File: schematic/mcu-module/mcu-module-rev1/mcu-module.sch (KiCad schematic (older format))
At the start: 22 parts, among them P1 MCU1, P2 MICROSD-SDIO-CD, P3 SWD, P4 MCU2, U1 STM32F103RE, X1 32768Hz, X2 8MHz

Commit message: MCU connectors created
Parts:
- removed P1: MCU1, ~, symbol CONN_20
- removed P4: MCU2, ~, symbol CONN_20
- added P1: MCU1, ~, symbol MCU1
- added P4: MCU2, ~, symbol MCU2
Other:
- moved on the sheet: C1, C10, C2, C3, C4, C5, C6, C7, C8, C9, P2, P3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

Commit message: MCU module rev2 done
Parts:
- added FB1: FILTER, ~, symbol FILTER
- C2, C3: value 100pF -> 20pF
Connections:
- net +3.3V: now also FB1.2; no longer P1.2 (P2)
- new net: FB1.1, P1.2 (P2)
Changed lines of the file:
@@
 Sheet 1 1
 Title "Caustic LT MCU boart"
-Date "27 may 2015"
+Date "14 nov 2015"
 Rev "1.0"
 Comp ""
@@
 P 5950 3400
 F 0 "C2" H 5950 3500 40  0000 L CNN
-F 1 "100pF" H 5956 3315 40  0000 L CNN
+F 1 "20pF" H 5956 3315 40  0000 L CNN
 F 2 "~" H 5988 3250 30  0000 C CNN
 F 3 "~" H 5950 3400 60  0000 C CNN
@@
 P 5950 3650
 F 0 "C3" H 5950 3750 40  0000 L CNN
-F 1 "100pF" H 5956 3565 40  0000 L CNN
+F 1 "20pF" H 5956 3565 40  0000 L CNN
 F 2 "~" H 5988 3500 30  0000 C CNN
 F 3 "~" H 5950 3650 60  0000 C CNN
@@
 L +3.3V #PWR014
 U 1 1 55643F60
-P 4650 1700
-F 0 "#PWR014" H 4650 1660 30  0001 C CNN
-F 1 "+3.3V" H 4650 1810 30  0000 C CNN
-F 2 "" H 4650 1700 60  0000 C CNN
-F 3 "" H 4650 1700 60  0000 C CNN
-	1    4650 1700
+P 5050 800
+F 0 "#PWR014" H 5050 760 30  0001 C CNN
+F 1 "+3.3V" H 5050 910 30  0000 C CNN
+F 2 "" H 5050 800 60  0000 C CNN
+F 3 "" H 5050 800 60  0000 C CNN
+	1    5050 800
 	0    1    1    0
 $EndComp
@@
 	5950 5450 6100 5450
 Connection ~ 6000 5450
-Wire Wire Line
-	5550 5450 5450 5450
 Connection ~ 5450 5450
 Wire Wire Line
@@
 	5850 2100 4350 2100
 Wire Wire Line
-	4350 1700 4650 1700
+	4350 1700 4900 1700
 Wire Wire Line
 	4350 1600 4450 1600
@@
 	1    0    0    -1
 $EndComp
+Wire Wire Line
+	5550 5450 5450 5450
+$Comp
+L FILTER FB1
+U 1 1 564783BA
+P 4900 1250
+F 0 "FB1" H 4900 1400 60  0000 C CNN
+F 1 "FILTER" H 4900 1150 60  0000 C CNN
+F 2 "~" H 4900 1250 60  0000 C CNN
+F 3 "~" H 4900 1250 60  0000 C CNN
+	1    4900 1250
+	0    -1   -1   0
+$EndComp
+Wire Wire Line
+	4900 1700 4900 1600
+Wire Wire Line
+	4900 900  4900 800
+Wire Wire Line
+	4900 800  5050 800
 $EndSCHEMATC

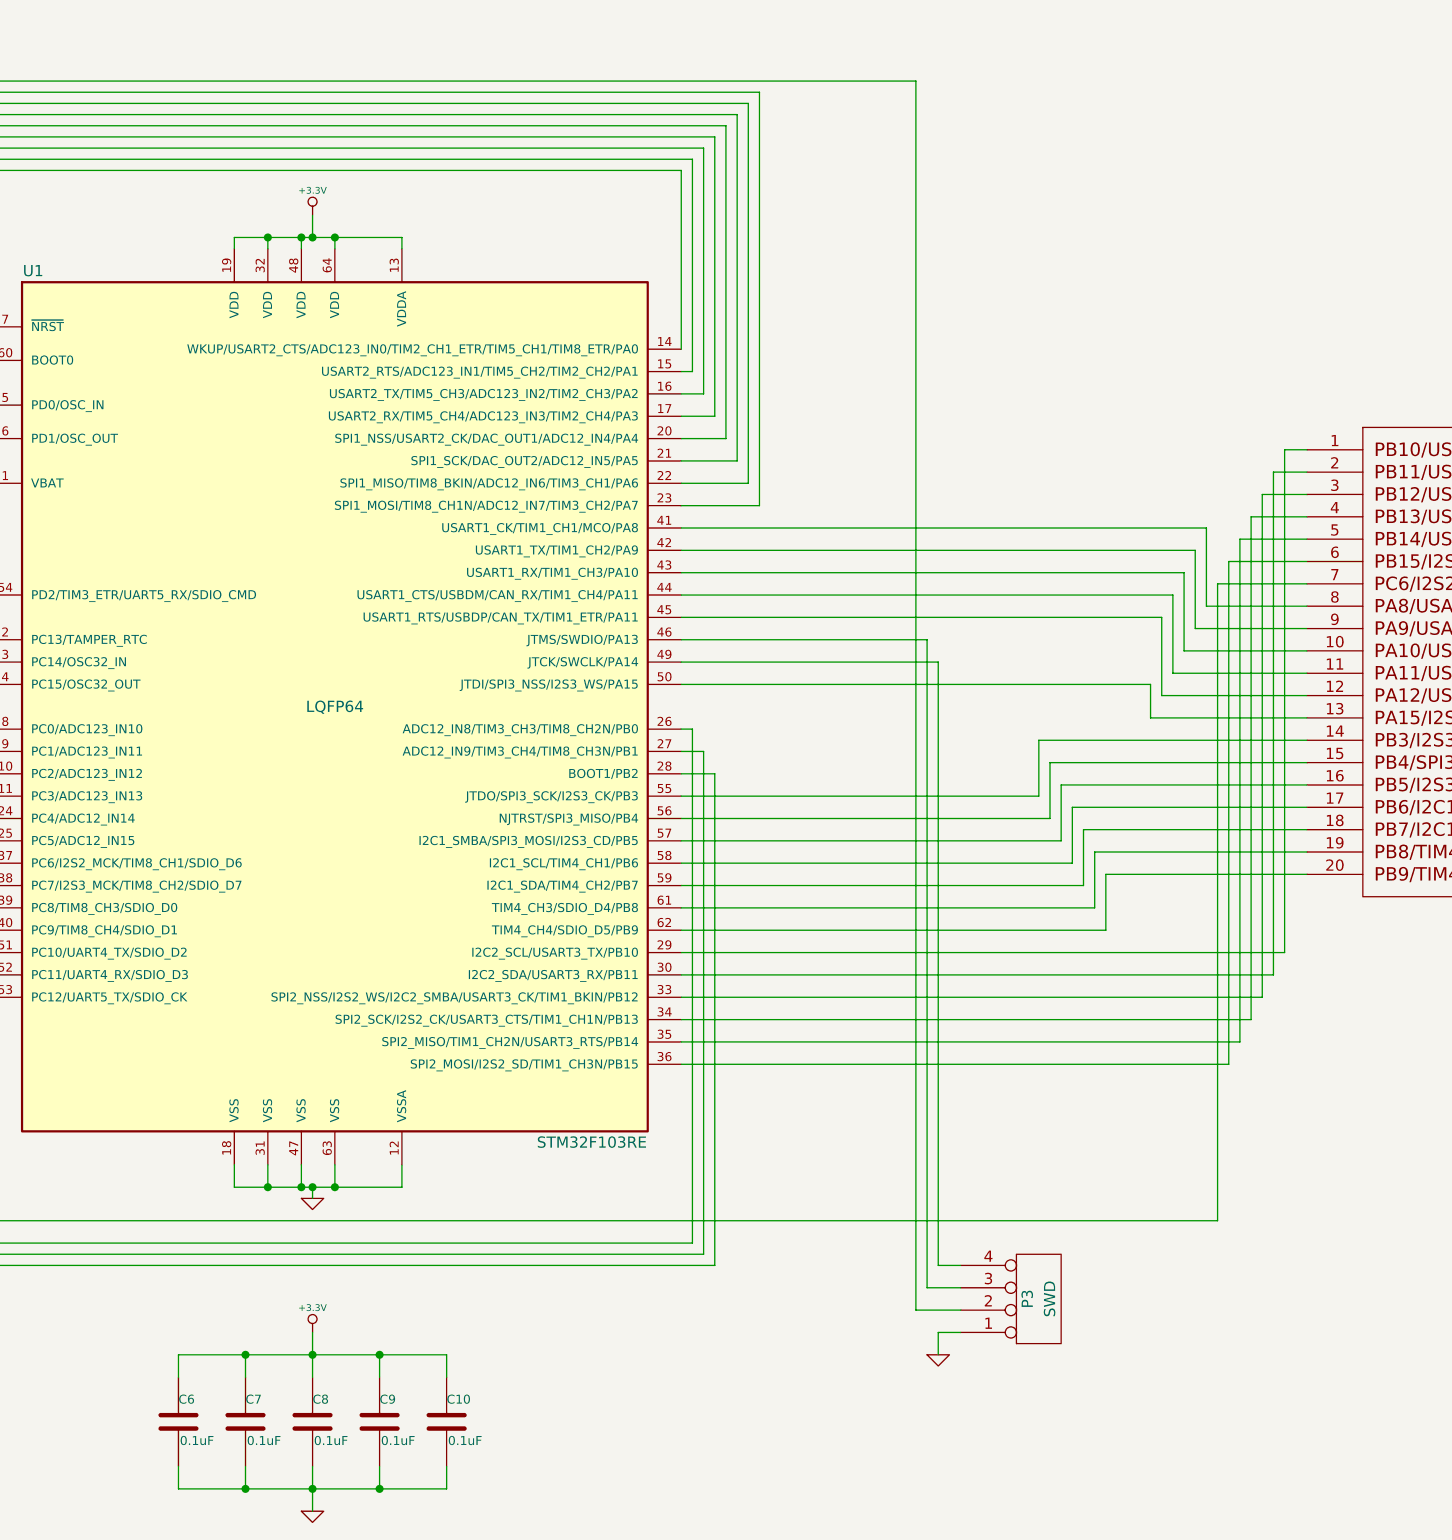
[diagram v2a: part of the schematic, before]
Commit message: Ferrite bead added to MCU module
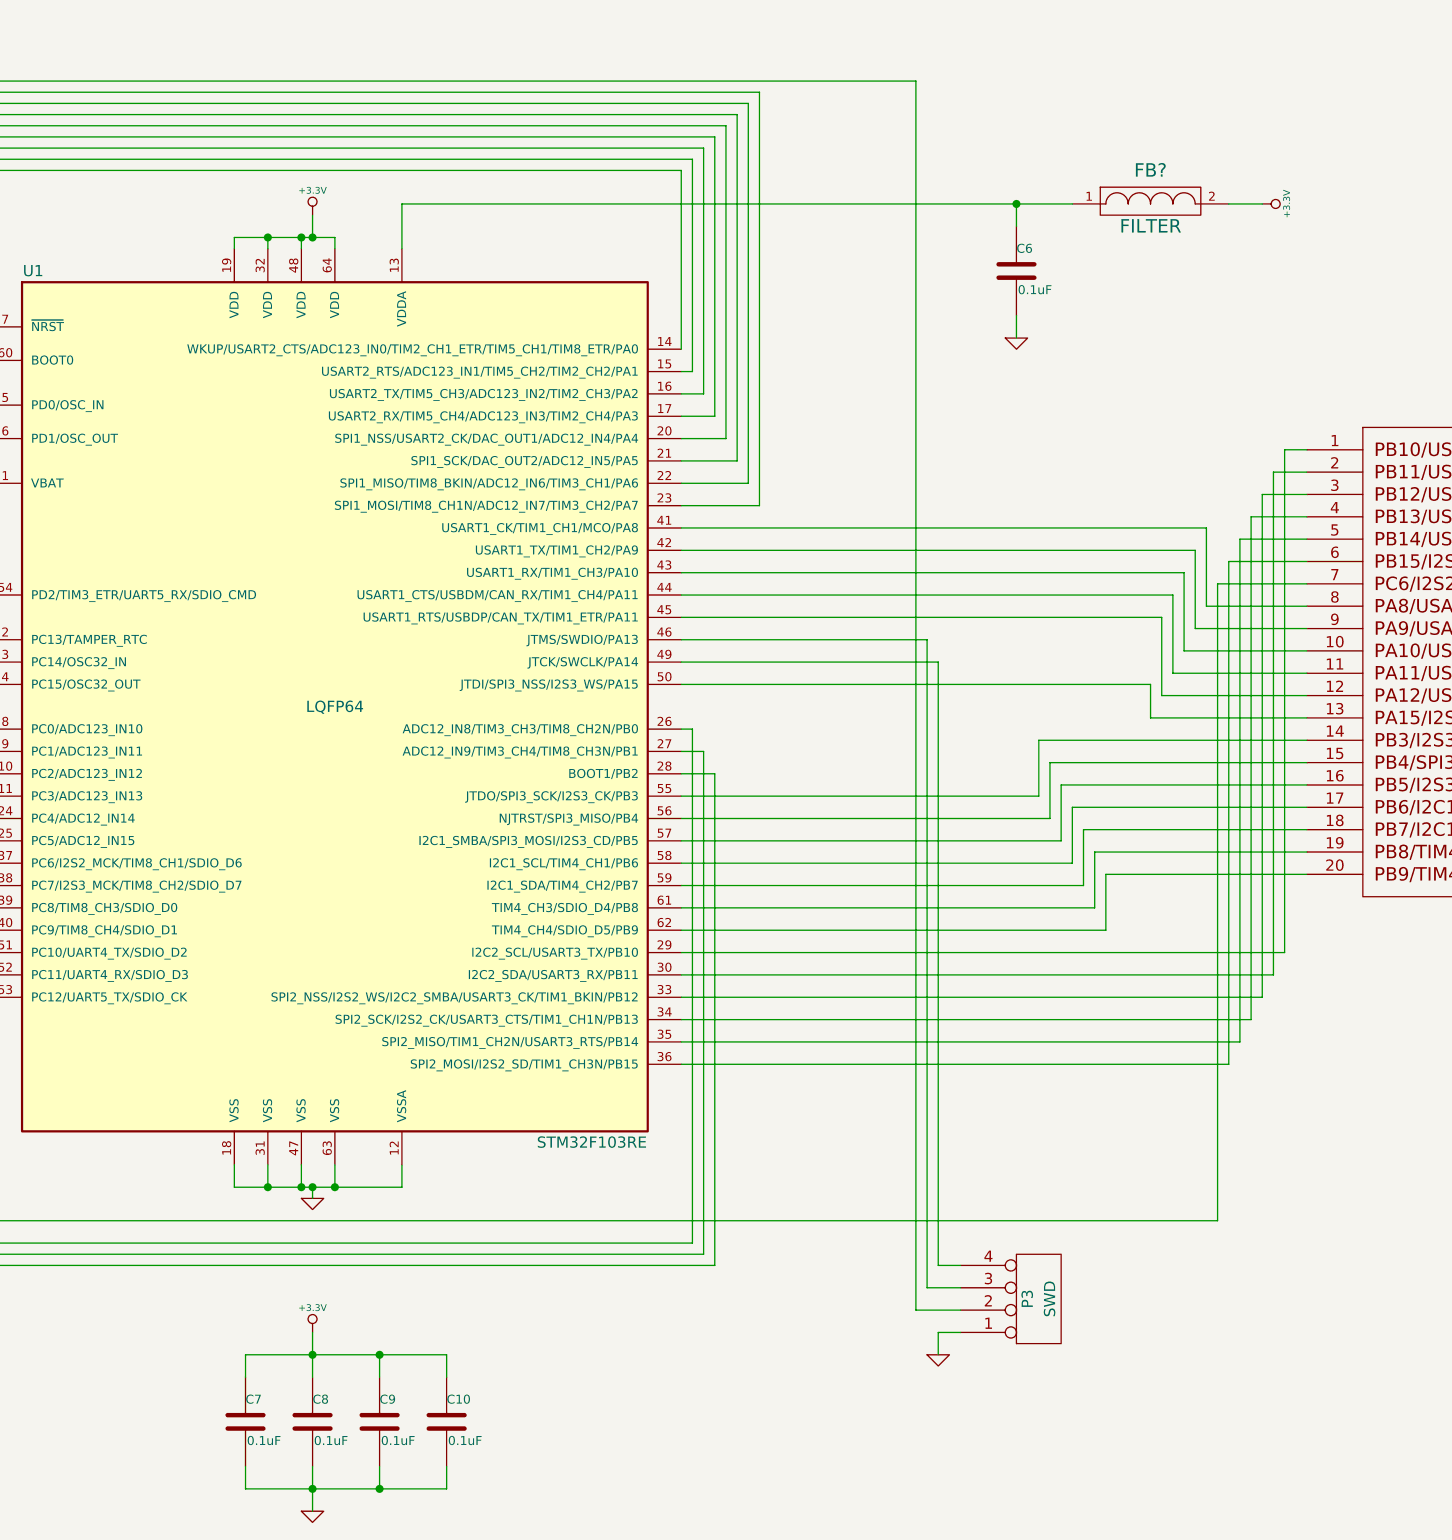
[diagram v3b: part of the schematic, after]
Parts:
- added FB?: FILTER, ~, symbol FILTER
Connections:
- net +3.3V: now also FB?.2; no longer C6.1, U1.13 (VDDA)
- new net: C6.1, FB?.1, U1.13 (VDDA)
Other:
- moved on the sheet: C6
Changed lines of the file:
@@
 Sheet 1 1
 Title "Caustic LT MCU boart"
-Date "14 nov 2015"
+Date "24 jan 2016"
 Rev "1.0"
 Comp ""
@@
 L C C6
 U 1 1 55641DCE
-P 8150 7000
-F 0 "C6" H 8150 7100 40  0000 L CNN
-F 1 "0.1uF" H 8156 6915 40  0000 L CNN
-F 2 "~" H 8188 6850 30  0000 C CNN
-F 3 "~" H 8150 7000 60  0000 C CNN
-	1    8150 7000
+P 11900 1850
+F 0 "C6" H 11900 1950 40  0000 L CNN
+F 1 "0.1uF" H 11906 1765 40  0000 L CNN
+F 2 "~" H 11938 1700 30  0000 C CNN
+F 3 "~" H 11900 1850 60  0000 C CNN
+	1    11900 1850
 	1    0    0    -1
 $EndComp
@@
 $EndComp
 Wire Wire Line
-	8150 6800 8150 6700
-Wire Wire Line
-	8150 6700 9350 6700
-Wire Wire Line
 	9350 6700 9350 6800
 Wire Wire Line
 	8450 6800 8450 6700
-Connection ~ 8450 6700
 Wire Wire Line
 	8750 6600 8750 6800
-Connection ~ 8750 6700
-Wire Wire Line
-	9050 6800 9050 6700
-Connection ~ 9050 6700
-Wire Wire Line
-	8150 7200 8150 7300
-Wire Wire Line
-	8150 7300 9350 7300
+Wire Wire Line
+	9050 6700 9050 6800
 Wire Wire Line
 	9350 7300 9350 7200
 Wire Wire Line
 	8450 7200 8450 7300
-Connection ~ 8450 7300
 Wire Wire Line
 	8750 7200 8750 7400
-Connection ~ 8750 7300
-Wire Wire Line
-	9050 7200 9050 7300
-Connection ~ 9050 7300
+Wire Wire Line
+	9050 7300 9050 7200
 Wire Wire Line
 	8400 5850 8400 5950
@@
 	8400 1750 8400 1700
 Wire Wire Line
-	8400 1700 9150 1700
-Wire Wire Line
-	9150 1700 9150 1750
+	9150 1550 9150 1750
 Wire Wire Line
 	8550 1750 8550 1700
-Connection ~ 8550 1700
-Wire Wire Line
-	8700 1750 8700 1700
-Connection ~ 8700 1700
-Wire Wire Line
-	8850 1750 8850 1700
-Connection ~ 8850 1700
-Wire Wire Line
-	8750 1600 8750 1700
-Connection ~ 8750 1700
+Wire Wire Line
+	8700 1700 8700 1750
+Wire Wire Line
+	8850 1700 8850 1750
+Wire Wire Line
+	8750 1700 8750 1600
 Wire Wire Line
 	7100 1900 6750 1900
@@
 Wire Wire Line
 	4900 800  5050 800
+Wire Wire Line
+	8450 6700 9350 6700
+Connection ~ 8750 6700
+Connection ~ 9050 6700
+Wire Wire Line
+	8450 7300 9350 7300
+Connection ~ 8750 7300
+Connection ~ 9050 7300
+$Comp
+L GND #PWR?
+U 1 1 56A481F6
+P 11900 2150
+F 0 "#PWR?" H 11900 2150 30  0001 C CNN
+F 1 "GND" H 11900 2080 30  0001 C CNN
+F 2 "" H 11900 2150 60  0000 C CNN
+F 3 "" H 11900 2150 60  0000 C CNN
+	1    11900 2150
+	1    0    0    -1
+$EndComp
+Wire Wire Line
+	8400 1700 8850 1700
+Connection ~ 8550 1700
+Connection ~ 8700 1700
+Connection ~ 8750 1700
+$Comp
+L FILTER FB?
+U 1 1 56A4868A
+P 12500 1550
+F 0 "FB?" H 12500 1700 60  0000 C CNN
+F 1 "FILTER" H 12500 1450 60  0000 C CNN
+F 2 "~" H 12500 1550 60  0000 C CNN
+F 3 "~" H 12500 1550 60  0000 C CNN
+	1    12500 1550
+	1    0    0    -1
+$EndComp
+$Comp
+L +3.3V #PWR?
+U 1 1 56A48699
+P 13000 1550
+F 0 "#PWR?" H 13000 1510 30  0001 C CNN
+F 1 "+3.3V" H 13000 1660 30  0000 C CNN
+F 2 "" H 13000 1550 60  0000 C CNN
+F 3 "" H 13000 1550 60  0000 C CNN
+	1    13000 1550
+	0    1    1    0
+$EndComp
+Wire Wire Line
+	11900 1650 11900 1550
+Wire Wire Line
+	9150 1550 12150 1550
+Wire Wire Line
+	11900 2050 11900 2150
+Wire Wire Line
+	12850 1550 13000 1550
+Connection ~ 11900 1550
 $EndSCHEMATC

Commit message: Prev. commit fix
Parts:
- gave numbers to parts that had none: 1
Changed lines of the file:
@@
 Connection ~ 9050 7300
 $Comp
-L GND #PWR?
+L GND #PWR016
 U 1 1 56A481F6
 P 11900 2150
-F 0 "#PWR?" H 11900 2150 30  0001 C CNN
+F 0 "#PWR016" H 11900 2150 30  0001 C CNN
 F 1 "GND" H 11900 2080 30  0001 C CNN
 F 2 "" H 11900 2150 60  0000 C CNN
@@
 Connection ~ 8750 1700
 $Comp
-L FILTER FB?
+L FILTER FB2
 U 1 1 56A4868A
 P 12500 1550
-F 0 "FB?" H 12500 1700 60  0000 C CNN
+F 0 "FB2" H 12500 1700 60  0000 C CNN
 F 1 "FILTER" H 12500 1450 60  0000 C CNN
 F 2 "~" H 12500 1550 60  0000 C CNN
@@
 $EndComp
 $Comp
-L +3.3V #PWR?
+L +3.3V #PWR017
 U 1 1 56A48699
 P 13000 1550
-F 0 "#PWR?" H 13000 1510 30  0001 C CNN
+F 0 "#PWR017" H 13000 1510 30  0001 C CNN
 F 1 "+3.3V" H 13000 1660 30  0000 C CNN
 F 2 "" H 13000 1550 60  0000 C CNN
